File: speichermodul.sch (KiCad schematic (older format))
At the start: 11 parts, among them U1 7400, U2 74LS08

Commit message: additions and corrections
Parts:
- removed JP? (x3): JUMPER, ~, symbol JUMPER
- removed U?: 7400, ~, symbol 7400
- added C?: C, ~, symbol C
- added D? (x2): LED, ~, symbol LED
- added P?: CONN_3X2, symbol CONN_3X2
- added R?: 10k, ~, symbol R
- added R? (x4): R, ~, symbol R
- added SW? (x2): SW_PUSH, ~, symbol SW_PUSH
- added unit 4 of U1
- added U3: 74LS08, ~, symbol 74LS08
- added U4: 74LS14, ~, symbol 74LS14
- R1: value R -> 1,7k
- gave numbers to parts that had none: 1
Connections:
- net labels added: EN-IN, GND, VCC, _auto
- wire segments 15 -> 61
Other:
- moved on the sheet: IC?, R1, R2, R3, U1A, U1B, U1C, U2A, U2B, U2C, U2D

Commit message: switch to kicad 4
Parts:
- removed R?: 10k, ~, symbol R
- added R? (x2): 4,7k, ~, symbol R
- added RP?: R_PACK4, ~, symbol R_PACK4
- gave numbers to parts that had none: 11
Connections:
- net labels added: _WR
- wire segments 61 -> 71
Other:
- moved on the sheet: D2, P1, R8, U4C
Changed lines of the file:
@@
 LIBS:memory
 LIBS:xilinx
-LIBS:special
 LIBS:microcontrollers
 LIBS:dsp
@@
 Sheet 1 1
 Title "speichermodul"
-Date "9 sep 2016"
+Date "10 sep 2016"
 Rev ""
 Comp ""
@@
 $EndComp
 $Comp
-L 6116 IC?
+L 6116 IC1
 U 1 1 57D2A745
 P 10250 3350
-F 0 "IC?" H 9850 4150 40  0000 C CNN
+F 0 "IC1" H 9850 4150 40  0000 C CNN
 F 1 "6116" H 10600 2550 40  0000 C CNN
 F 2 "" H 10250 3350 60  0000 C CNN
@@
 	4    1900 4150
 	1    0    0    -1
-$EndComp
-$Comp
-L R R?
-U 1 1 57D2D569
-P 6500 2150
-F 0 "R?" V 6580 2150 40  0000 C CNN
-F 1 "10k" V 6507 2151 40  0000 C CNN
-F 2 "~" V 6430 2150 30  0000 C CNN
-F 3 "~" H 6500 2150 30  0000 C CNN
-	1    6500 2150
-	0    -1   -1   0
 $EndComp
 $Comp
@@
 L 74LS14 U4
 U 3 1 57D2D812
-P 9300 4850
-F 0 "U4" H 9450 4950 40  0000 C CNN
-F 1 "74LS14" H 9500 4750 40  0000 C CNN
-F 2 "~" H 9300 4850 60  0000 C CNN
-F 3 "~" H 9300 4850 60  0000 C CNN
-	3    9300 4850
+P 8450 4850
+F 0 "U4" H 8600 4950 40  0000 C CNN
+F 1 "74LS14" H 8650 4750 40  0000 C CNN
+F 2 "~" H 8450 4850 60  0000 C CNN
+F 3 "~" H 8450 4850 60  0000 C CNN
+	3    8450 4850
 	0    1    1    0
 $EndComp
 $Comp
-L R R?
+L R R7
 U 1 1 57D2D821
 P 7950 5700
-F 0 "R?" V 8030 5700 40  0000 C CNN
+F 0 "R7" V 8030 5700 40  0000 C CNN
 F 1 "R" V 7957 5701 40  0000 C CNN
 F 2 "~" V 7880 5700 30  0000 C CNN
@@
 $EndComp
 $Comp
-L R R?
+L R R8
 U 1 1 57D2D830
-P 9300 5700
-F 0 "R?" V 9380 5700 40  0000 C CNN
-F 1 "R" V 9307 5701 40  0000 C CNN
-F 2 "~" V 9230 5700 30  0000 C CNN
-F 3 "~" H 9300 5700 30  0000 C CNN
-	1    9300 5700
-	1    0    0    -1
-$EndComp
-$Comp
-L R R?
+P 8450 5700
+F 0 "R8" V 8530 5700 40  0000 C CNN
+F 1 "R" V 8457 5701 40  0000 C CNN
+F 2 "~" V 8380 5700 30  0000 C CNN
+F 3 "~" H 8450 5700 30  0000 C CNN
+	1    8450 5700
+	1    0    0    -1
+$EndComp
+$Comp
+L R R6
 U 1 1 57D2D83F
 P 6550 7350
-F 0 "R?" V 6630 7350 40  0000 C CNN
+F 0 "R6" V 6630 7350 40  0000 C CNN
 F 1 "R" V 6557 7351 40  0000 C CNN
 F 2 "~" V 6480 7350 30  0000 C CNN
@@
 $EndComp
 $Comp
-L R R?
+L R R5
 U 1 1 57D2D84E
 P 6550 5650
-F 0 "R?" V 6630 5650 40  0000 C CNN
+F 0 "R5" V 6630 5650 40  0000 C CNN
 F 1 "R" V 6557 5651 40  0000 C CNN
 F 2 "~" V 6480 5650 30  0000 C CNN
@@
 $EndComp
 $Comp
-L C C?
+L C C1
 U 1 1 57D2D85D
 P 6000 6000
-F 0 "C?" H 6000 6100 40  0000 L CNN
+F 0 "C1" H 6000 6100 40  0000 L CNN
 F 1 "C" H 6006 5915 40  0000 L CNN
 F 2 "~" H 6038 5850 30  0000 C CNN
@@
 $EndComp
 $Comp
-L LED D?
+L LED D1
 U 1 1 57D2D86C
 P 7950 6250
-F 0 "D?" H 7950 6350 50  0000 C CNN
+F 0 "D1" H 7950 6350 50  0000 C CNN
 F 1 "LED" H 7950 6150 50  0000 C CNN
 F 2 "~" H 7950 6250 60  0000 C CNN
@@
 $EndComp
 $Comp
-L LED D?
+L LED D2
 U 1 1 57D2D87B
-P 9300 6250
-F 0 "D?" H 9300 6350 50  0000 C CNN
-F 1 "LED" H 9300 6150 50  0000 C CNN
-F 2 "~" H 9300 6250 60  0000 C CNN
-F 3 "~" H 9300 6250 60  0000 C CNN
-	1    9300 6250
+P 8450 6250
+F 0 "D2" H 8450 6350 50  0000 C CNN
+F 1 "LED" H 8450 6150 50  0000 C CNN
+F 2 "~" H 8450 6250 60  0000 C CNN
+F 3 "~" H 8450 6250 60  0000 C CNN
+	1    8450 6250
 	0    1    1    0
 $EndComp
@@
 $EndComp
 $Comp
-L SW_PUSH SW?
+L SW_PUSH SW2
 U 1 1 57D2F144
 P 1000 4850
-F 0 "SW?" H 1150 4960 50  0000 C CNN
+F 0 "SW2" H 1150 4960 50  0000 C CNN
 F 1 "SW_PUSH" H 1000 4770 50  0000 C CNN
 F 2 "~" H 1000 4850 60  0000 C CNN
@@
 $EndComp
 $Comp
-L SW_PUSH SW?
+L SW_PUSH SW1
 U 1 1 57D2F1B1
 P 1000 2650
-F 0 "SW?" H 1150 2760 50  0000 C CNN
+F 0 "SW1" H 1150 2760 50  0000 C CNN
 F 1 "SW_PUSH" H 1000 2570 50  0000 C CNN
 F 2 "~" H 1000 2650 60  0000 C CNN
@@
 L GND #PWR012
 U 1 1 57D2FC3C
-P 9300 6600
-F 0 "#PWR012" H 9300 6600 30  0001 C CNN
-F 1 "GND" H 9300 6530 30  0001 C CNN
-F 2 "" H 9300 6600 60  0000 C CNN
-F 3 "" H 9300 6600 60  0000 C CNN
-	1    9300 6600
-	1    0    0    -1
-$EndComp
-Wire Wire Line
-	9300 6600 9300 6450
-Wire Wire Line
-	9300 6050 9300 5950
-Wire Wire Line
-	9300 5450 9300 5300
+P 8450 6600
+F 0 "#PWR012" H 8450 6600 30  0001 C CNN
+F 1 "GND" H 8450 6530 30  0001 C CNN
+F 2 "" H 8450 6600 60  0000 C CNN
+F 3 "" H 8450 6600 60  0000 C CNN
+	1    8450 6600
+	1    0    0    -1
+$EndComp
+Wire Wire Line
+	8450 6600 8450 6450
+Wire Wire Line
+	8450 6050 8450 5950
+Wire Wire Line
+	8450 5450 8450 5300
 Wire Wire Line
 	7950 5450 7950 5300
@@
 	7850 3950 9650 3950
 Wire Wire Line
-	9300 3950 9300 4400
+	8450 3950 8450 4400
 Wire Wire Line
 	7850 3150 8050 3150
@@
 Connection ~ 7950 3150
 Wire Wire Line
-	8050 3350 8050 3950
+	8050 3950 8050 3350
 Connection ~ 8050 3950
 Wire Wire Line
-	9250 3250 9400 3250
-Wire Wire Line
-	9400 3250 9400 4050
-Wire Wire Line
-	9400 4050 9650 4050
-Connection ~ 9300 3950
-$Comp
-L CONN_3X2 P?
+	9250 4050 9650 4050
+Wire Wire Line
+	9250 3250 9250 4050
+$Comp
+L CONN_3X2 P1
 U 1 1 57D30104
-P 8900 2500
-F 0 "P?" H 8900 2750 50  0000 C CNN
-F 1 "CONN_3X2" V 8900 2550 40  0000 C CNN
-F 2 "" H 8900 2500 60  0000 C CNN
-F 3 "" H 8900 2500 60  0000 C CNN
-	1    8900 2500
-	1    0    0    -1
-$EndComp
+P 8650 2700
+F 0 "P1" H 8650 2950 50  0000 C CNN
+F 1 "CONN_3X2" V 8650 2750 40  0000 C CNN
+F 2 "" H 8650 2700 60  0000 C CNN
+F 3 "" H 8650 2700 60  0000 C CNN
+	1    8650 2700
+	1    0    0    -1
+$EndComp
+Wire Wire Line
+	6650 3050 6650 2550
+$Comp
+L R R?
+U 1 1 57D39944
+P 6400 2550
+F 0 "R?" V 6480 2550 40  0000 C CNN
+F 1 "4,7k" V 6407 2551 40  0000 C CNN
+F 2 "~" V 6330 2550 30  0000 C CNN
+F 3 "~" H 6400 2550 30  0000 C CNN
+	1    6400 2550
+	0    -1   -1   0
+$EndComp
+$Comp
+L VCC #PWR?
+U 1 1 57D39958
+P 5950 2550
+F 0 "#PWR?" H 5950 2650 30  0001 C CNN
+F 1 "VCC" H 5950 2650 30  0000 C CNN
+F 2 "" H 5950 2550 60  0000 C CNN
+F 3 "" H 5950 2550 60  0000 C CNN
+	1    5950 2550
+	0    -1   -1   0
+$EndComp
+Wire Wire Line
+	6150 2550 5950 2550
+Connection ~ 8450 3950
+Entry Wire Line
+	9550 3550 9650 3650
+Entry Wire Line
+	9550 3450 9650 3550
+Entry Wire Line
+	9550 3550 9650 3650
+Entry Wire Line
+	9550 3350 9650 3450
+Entry Wire Line
+	9050 2550 9150 2650
+Entry Wire Line
+	9050 2650 9150 2750
+Entry Wire Line
+	9050 2750 9150 2850
+Wire Bus Line
+	9150 2650 9150 3050
+Wire Bus Line
+	9150 3050 9400 3050
+Wire Bus Line
+	9400 3050 9400 3350
+Wire Bus Line
+	9400 3350 9550 3350
+Wire Bus Line
+	9550 3350 9550 3550
+$Comp
+L GND #PWR?
+U 1 1 57D39B92
+P 8150 2850
+F 0 "#PWR?" H 8150 2850 30  0001 C CNN
+F 1 "GND" H 8150 2780 30  0001 C CNN
+F 2 "" H 8150 2850 60  0000 C CNN
+F 3 "" H 8150 2850 60  0000 C CNN
+	1    8150 2850
+	1    0    0    -1
+$EndComp
+Wire Wire Line
+	8150 2850 8150 2550
+Wire Wire Line
+	8150 2550 8250 2550
+Wire Wire Line
+	8250 2650 8150 2650
+Connection ~ 8150 2650
+Wire Wire Line
+	8250 2750 8150 2750
+Connection ~ 8150 2750
+$Comp
+L R_PACK4 RP?
+U 1 1 57D39DF4
+P 9150 2050
+F 0 "RP?" H 9150 2500 40  0000 C CNN
+F 1 "R_PACK4" H 9150 2000 40  0000 C CNN
+F 2 "~" H 9150 2050 60  0000 C CNN
+F 3 "~" H 9150 2050 60  0000 C CNN
+	1    9150 2050
+	1    0    0    -1
+$EndComp
+$Comp
+L R R?
+U 1 1 57D39F23
+P 7200 4500
+F 0 "R?" V 7280 4500 40  0000 C CNN
+F 1 "4,7k" V 7207 4501 40  0000 C CNN
+F 2 "~" V 7130 4500 30  0000 C CNN
+F 3 "~" H 7200 4500 30  0000 C CNN
+	1    7200 4500
+	0    -1   -1   0
+$EndComp
+$Comp
+L VCC #PWR?
+U 1 1 57D39F37
+P 7550 4450
+F 0 "#PWR?" H 7550 4550 30  0001 C CNN
+F 1 "VCC" H 7550 4550 30  0000 C CNN
+F 2 "" H 7550 4450 60  0000 C CNN
+F 3 "" H 7550 4450 60  0000 C CNN
+	1    7550 4450
+	1    0    0    -1
+$EndComp
+Wire Wire Line
+	6650 4050 6650 4500
+Wire Wire Line
+	6650 4500 6950 4500
+Wire Wire Line
+	7450 4500 7550 4500
+Wire Wire Line
+	7550 4500 7550 4450
+Wire Wire Line
+	6850 4500 6850 4700
+Connection ~ 6850 4500
+Text Label 6750 4600 0    60   ~ 0
+_WR
 $EndSCHEMATC

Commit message: schematic almoust finished
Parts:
- removed RP?: R_PACK4, ~, symbol R_PACK4
- added D10, D11, D12, D13, D14, D15, D16, D17, D18, D3, D4, D5, D6, D7, D8, D9: LED, symbol LED
- added P2, P3, P4, P5, P6, P7: CONN_01X01, symbol CONN_01X01
- added P8, P9: CONN_02X10, symbol CONN_02X10
- added R10, R11, R12, R13, R14, R15, R16, R17, R18, R19, R20, R21, R22, R23, R4, R9: 330, symbol R
- added RP1: R_PACK4BUSSED, symbol R_PACK4BUSSED
- added U5, U6: 74LS540, symbol 74LS540
- gave numbers to parts that had none: 2
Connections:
- net labels added: A0, A1, A10, A2, A3, A4, A5, A6, A7, A8, A9, D0, D1, D2, D3, D4, D5, D6, D7, _RD
- wire segments 71 -> 134
- no-connect marks 0 -> 1
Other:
- note added: "Adressbus"
- note added: "Datenbus"
- note added: "R Pack 8 Bussed fehlt hier noch"
- moved on the sheet: C1, D1, D2, R5, R6, R7, R8, U4B, U4C, U4F

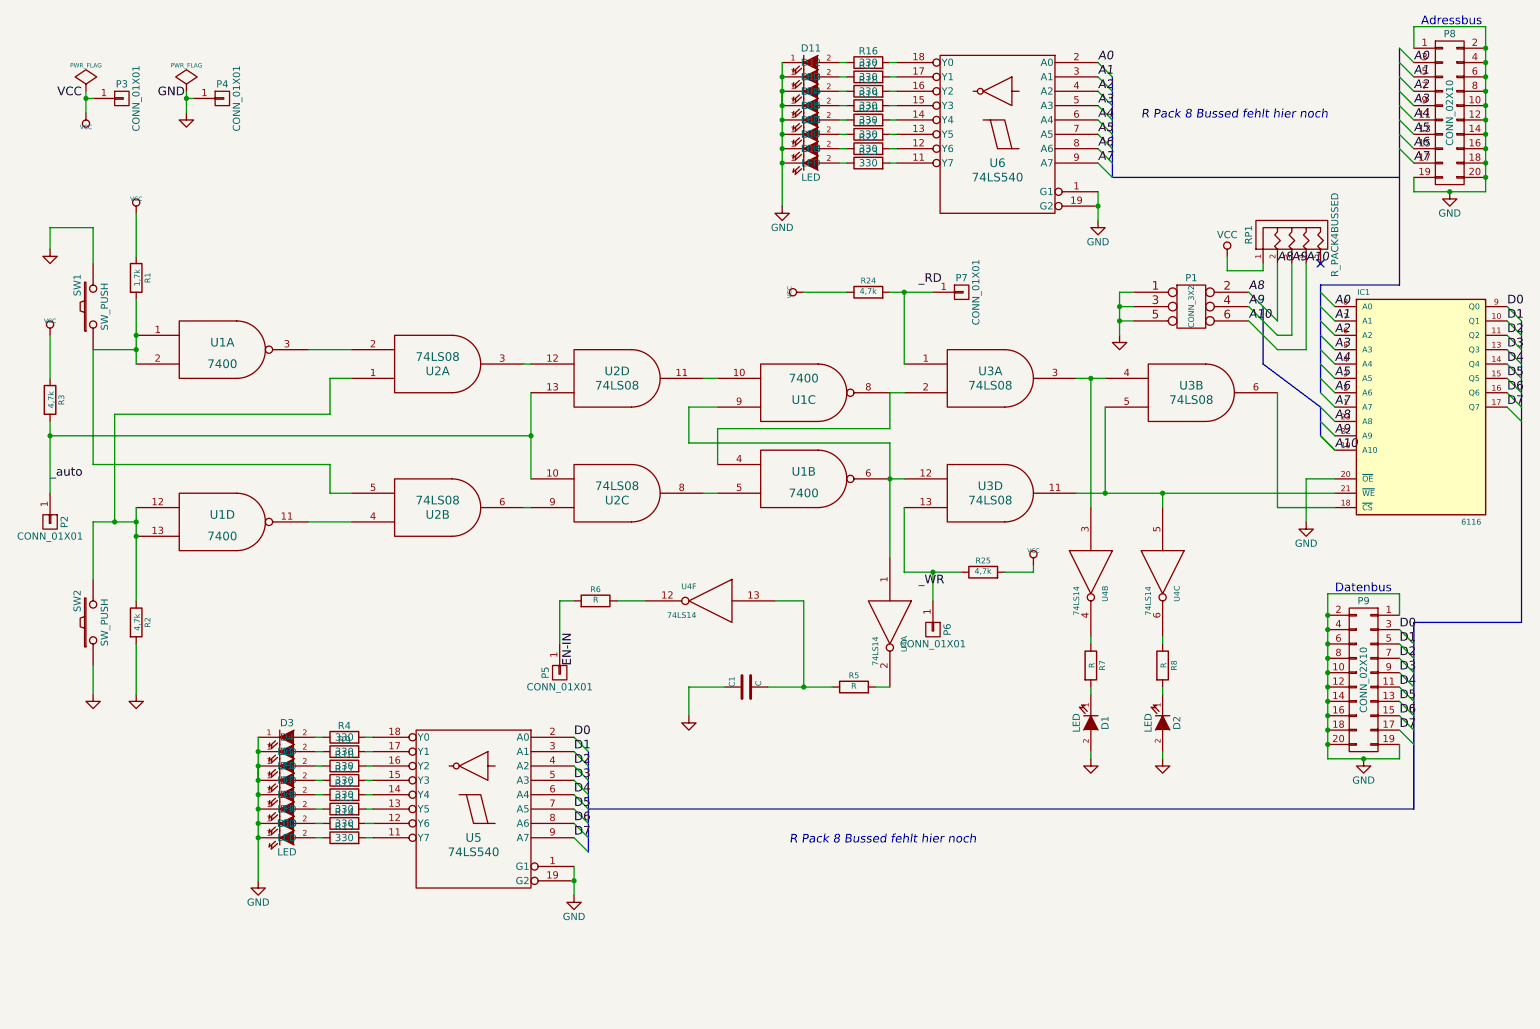
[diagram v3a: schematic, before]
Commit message: schematic completed
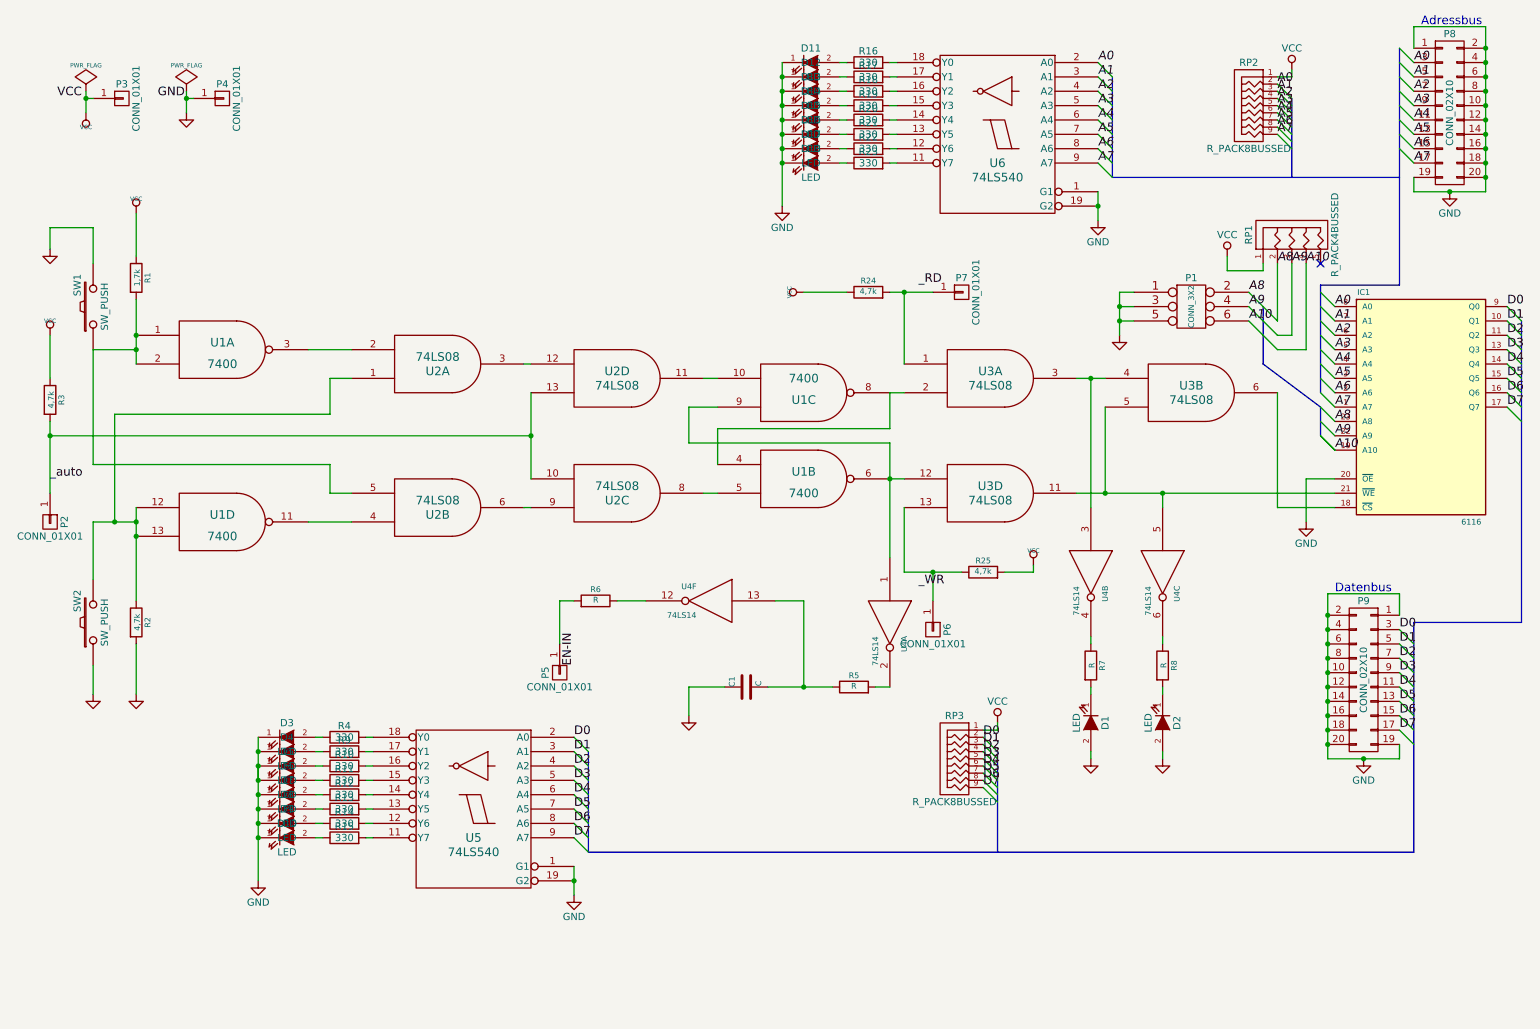
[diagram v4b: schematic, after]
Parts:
- added RP2, RP3: R_PACK8BUSSED, ~, symbol R_PACK8BUSSED
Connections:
- net A0: now also RP2.2 (P2)
- net A1: now also RP2.3 (P3)
- net A2: now also RP2.4 (P4)
- net A3: now also RP2.5 (P5)
- net A4: now also RP2.6 (P6)
- net A5: now also RP2.7 (P7)
- net A6: now also RP2.8 (P8)
- net A7: now also RP2.9 (P9)
- net D0: now also RP3.2 (P2)
- net D1: now also RP3.3 (P3)
- net D2: now also RP3.4 (P4)
- net D3: now also RP3.5 (P5)
- net D4: now also RP3.6 (P6)
- net D5: now also RP3.7 (P7)
- net D6: now also RP3.8 (P8)
- net D7: now also RP3.9 (P9)
- net VCC: now also RP2.1 (P1), RP3.1 (P1)
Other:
- note removed: "R Pack 8 Bussed fehlt hier noch"
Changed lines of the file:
@@
 Sheet 1 1
 Title "speichermodul"
-Date "11 sep 2016"
+Date "13 sep 2016"
 Rev ""
 Comp ""
@@
 Text Label 4350 6350 0    60   ~ 0
 D7
-Text Notes 8300 1350 0    60   Italic 0
-R Pack 8 Bussed fehlt hier noch
-Text Notes 5850 6400 0    60   Italic 0
-R Pack 8 Bussed fehlt hier noch
 Text Label 9650 3450 0    60   Italic 0
 A8
@@
 	10950 4850 10200 4850
 Wire Bus Line
-	10200 4850 10200 6150
-Wire Bus Line
-	10200 6150 4450 6150
+	10200 4850 10200 6450
 Wire Bus Line
 	4450 5750 4450 6450
@@
 Wire Bus Line
 	9150 3050 9550 3350
+$Comp
+L R_PACK8BUSSED RP2
+U 1 1 57D77728
+P 9050 1250
+F 0 "RP2" H 9050 1550 50  0000 C CNN
+F 1 "R_PACK8BUSSED" H 9050 950 50  0000 C CNN
+F 2 "~" H 9050 1300 60  0000 C CNN
+F 3 "~" H 9050 1300 60  0000 C CNN
+	1    9050 1250
+	-1   0    0    -1
+$EndComp
+Wire Bus Line
+	9350 1200 9350 1750
+$Comp
+L VCC #PWR024
+U 1 1 57D778D3
+P 9350 1000
+F 0 "#PWR024" H 9350 850 50  0001 C CNN
+F 1 "VCC" H 9350 1150 50  0000 C CNN
+F 2 "" H 9350 1000 60  0000 C CNN
+F 3 "" H 9350 1000 60  0000 C CNN
+	1    9350 1000
+	1    0    0    -1
+$EndComp
+Wire Wire Line
+	9350 1050 9350 1000
+$Comp
+L R_PACK8BUSSED RP3
+U 1 1 57D77ABD
+P 7000 5800
+F 0 "RP3" H 7000 6100 50  0000 C CNN
+F 1 "R_PACK8BUSSED" H 7000 5500 50  0000 C CNN
+F 2 "~" H 7000 5850 60  0000 C CNN
+F 3 "~" H 7000 5850 60  0000 C CNN
+	1    7000 5800
+	-1   0    0    -1
+$EndComp
+Wire Bus Line
+	7300 5750 7300 6450
+$Comp
+L VCC #PWR025
+U 1 1 57D77ACC
+P 7300 5550
+F 0 "#PWR025" H 7300 5400 50  0001 C CNN
+F 1 "VCC" H 7300 5700 50  0000 C CNN
+F 2 "" H 7300 5550 60  0000 C CNN
+F 3 "" H 7300 5550 60  0000 C CNN
+	1    7300 5550
+	1    0    0    -1
+$EndComp
+Wire Wire Line
+	7300 5600 7300 5550
+Wire Bus Line
+	4450 6450 10200 6450
+Entry Wire Line
+	7200 5650 7300 5750
+Entry Wire Line
+	7200 5700 7300 5800
+Entry Wire Line
+	7200 5750 7300 5850
+Entry Wire Line
+	7200 5800 7300 5900
+Entry Wire Line
+	7200 5850 7300 5950
+Entry Wire Line
+	7200 5900 7300 6000
+Entry Wire Line
+	7200 5950 7300 6050
+Entry Wire Line
+	7200 6000 7300 6100
+Wire Wire Line
+	7300 5600 7200 5600
+Text Label 7200 5650 0    60   ~ 0
+D0
+Text Label 7200 5700 0    60   ~ 0
+D1
+Text Label 7200 5750 0    60   ~ 0
+D2
+Text Label 7200 5800 0    60   ~ 0
+D3
+Text Label 7200 5850 0    60   ~ 0
+D4
+Text Label 7200 5900 0    60   ~ 0
+D5
+Text Label 7200 5950 0    60   ~ 0
+D6
+Text Label 7200 6000 0    60   ~ 0
+D7
+Entry Wire Line
+	9250 1100 9350 1200
+Entry Wire Line
+	9250 1150 9350 1250
+Entry Wire Line
+	9250 1200 9350 1300
+Entry Wire Line
+	9250 1250 9350 1350
+Entry Wire Line
+	9250 1300 9350 1400
+Entry Wire Line
+	9250 1350 9350 1450
+Entry Wire Line
+	9250 1400 9350 1500
+Entry Wire Line
+	9250 1450 9350 1550
+Wire Wire Line
+	9250 1050 9350 1050
+Text Label 9250 1100 0    60   ~ 0
+A0
+Text Label 9250 1150 0    60   ~ 0
+A1
+Text Label 9250 1200 0    60   ~ 0
+A2
+Text Label 9250 1250 0    60   ~ 0
+A3
+Text Label 9250 1300 0    60   ~ 0
+A4
+Text Label 9250 1350 0    60   ~ 0
+A5
+Text Label 9250 1400 0    60   ~ 0
+A6
+Text Label 9250 1450 0    60   ~ 0
+A7
 $EndSCHEMATC

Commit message: changed version to Nightly Development Build for missing footprints
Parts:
- C1, R24, R25, R3, R5, R6, R7, R8, SW1, SW2, U1, U2, U3, U4: footprint ~ -> (none)
- D1, D2: footprint ~ -> LEDs:LED-3MM
- D3: footprint (none) -> LEDs:LED-3MM
- IC1: symbol 6116 -> 6116-RESCUE-speichermodul
- P7: footprint (none) -> Housings_DIP:DIP-16_W7.62mm
- P8, P9: footprint (none) -> Connect:IDC_Header_Straight_20pins
- R1, R2: footprint ~ -> Discret:R3
- RP2, RP3: footprint ~ -> Housings_SIP:SIP9_Housing_BigPads
- U5, U6: footprint (none) -> Housings_DIP:DIP-20_W7.62mm_LongPads
